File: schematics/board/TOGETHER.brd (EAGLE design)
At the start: 22 x 22 mm, 12 parts

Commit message: Добавлена плата TOGETHER
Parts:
- added U$1, U$18, U$19, U$2, U$20, U$21, U$3, U$4: KCONNECT-, CanCubeSat:KCONNECT-
- moved 3V3 42.4 mm to (39.5, 32.5)
- moved C1 42.4 mm to (32.5, 38.5)
- moved C10 42.4 mm to (35.0, 38.5)
- moved LIS3MDL 42.4 mm to (33.0, 43.0)
- moved LSM6DS3 42.4 mm to (49.0, 43.0)
- moved PWR 42.4 mm to (41.0, 49.0)
- moved R1 42.4 mm to (41.0, 47.0)
- moved R101 42.4 mm to (47.0, 38.5)
- moved R102 42.4 mm to (49.5, 38.5)
- moved SCL 42.4 mm to (42.5, 32.5)
- moved GND 42.4 mm to (36.5, 33.8)
- moved SDA 42.4 mm to (45.5, 33.8)
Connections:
- net GND renamed GND1
- new net BUS+: U$1.1, U$1.2, U$1.3, U$1.4, U$18.1, U$18.2, U$18.3, U$18.4, U$20.1, U$20.2, U$20.3, U$20.4, U$3.1, U$3.2, U$3.3, U$3.4
- new net BUS-: U$19.1, U$19.2, U$19.3, U$19.4, U$2.1, U$2.2, U$2.3, U$2.4, U$21.1, U$21.2, U$21.3, U$21.4, U$4.1, U$4.2, U$4.3, U$4.4
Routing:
- net GND1: track 51.8 -> 22.0 mm
- net VDD: track 59.9 -> 56.7 mm
- added copper zone on layer 16, net BUS+
- added copper zone on layer 1, net BUS-
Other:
- board size 22 x 22 mm -> 82 x 82 mm

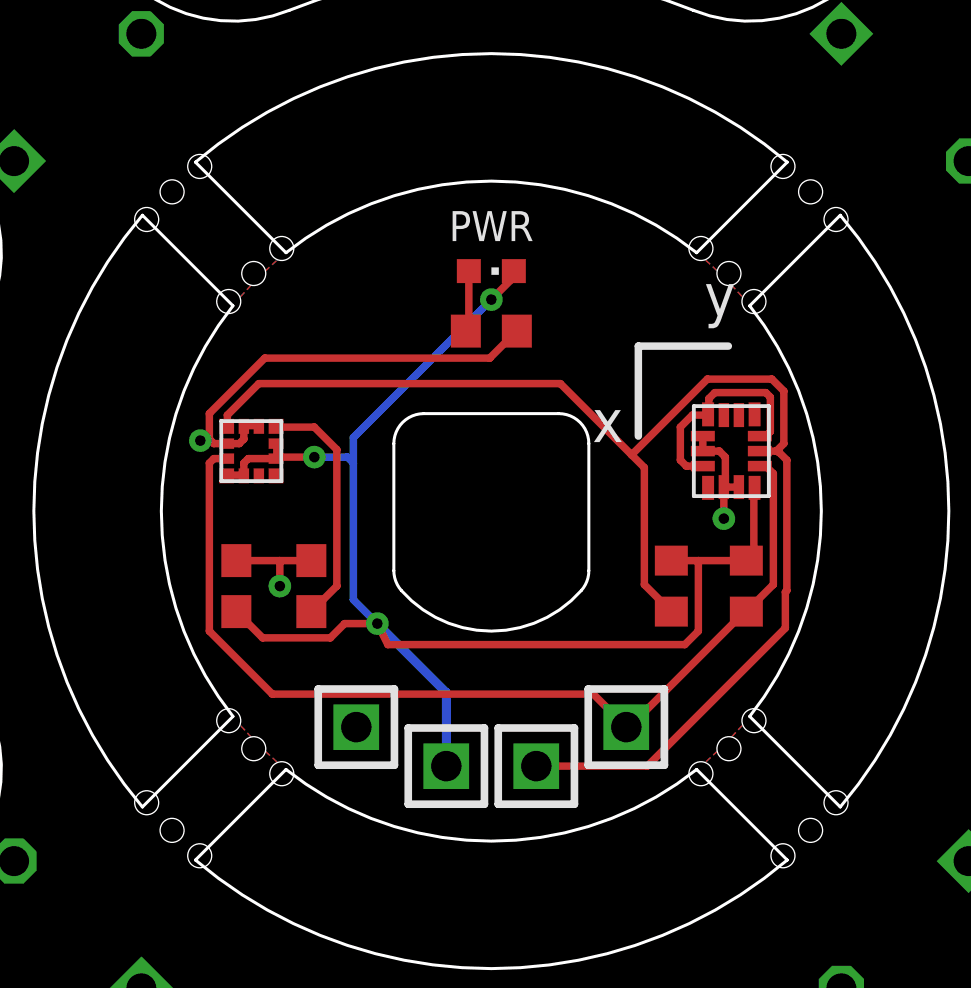
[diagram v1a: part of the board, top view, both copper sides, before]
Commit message: Исправлены MAG и BSK1
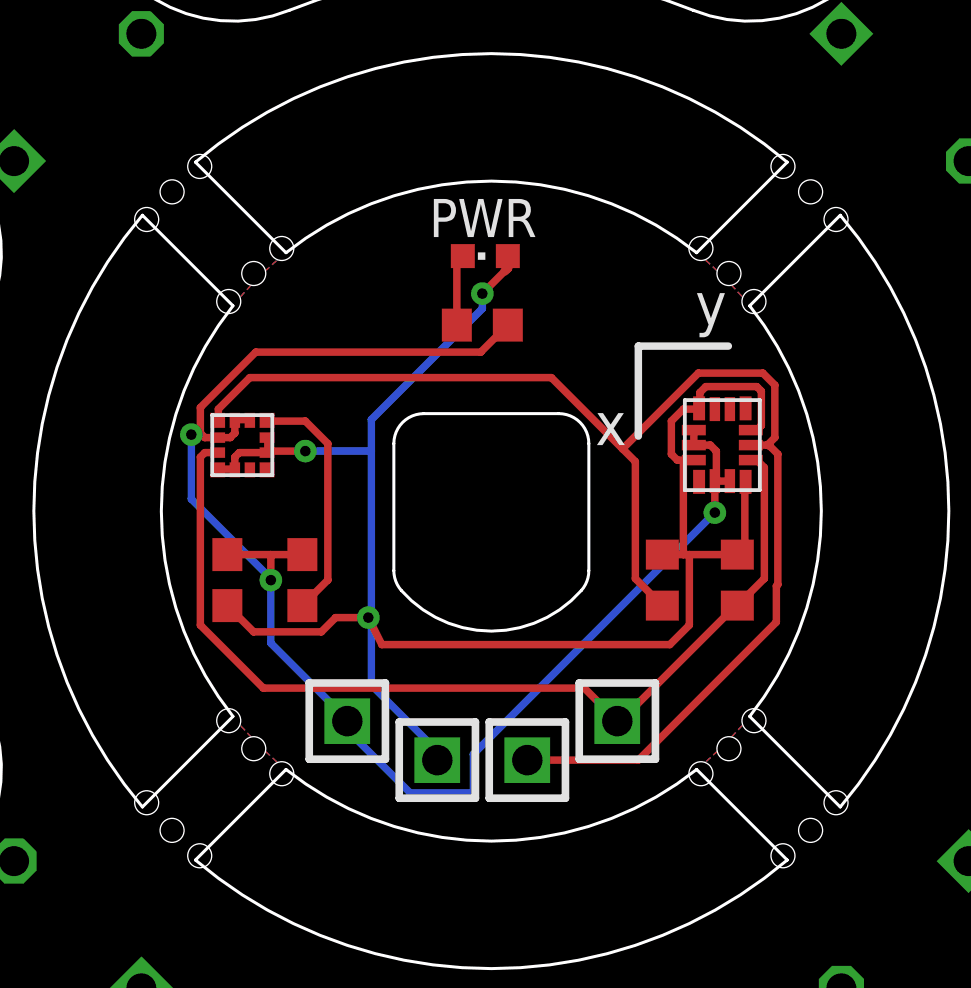
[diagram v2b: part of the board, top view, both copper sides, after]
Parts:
- moved PWR 0.54 mm to (40.8, 49.5), turned to 90 degrees
- moved 3V3 0.36 mm to (39.2, 32.7)
- moved C1 0.36 mm to (32.2, 38.7)
- moved C10 0.36 mm to (34.7, 38.7)
- moved GND 0.36 mm to (36.2, 34.0)
- moved LIS3MDL 0.36 mm to (32.7, 43.2)
- moved LSM6DS3 0.36 mm to (48.7, 43.2)
- moved R1 0.36 mm to (40.7, 47.2)
- moved R101 0.36 mm to (46.7, 38.7)
- moved R102 0.36 mm to (49.2, 38.7)
- moved SCL 0.36 mm to (42.2, 32.7)
- moved SDA 0.36 mm to (45.2, 34.0)
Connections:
- net GND1 renamed GND
- removed net N$37: PWR.A, R1.2
- removed net VDD: 3V3.1, C1.1, LIS3MDL.P$1, LIS3MDL.P$2, LIS3MDL.P$5, LIS3MDL.P$6, LSM6DS3.P$11, LSM6DS3.P$14, LSM6DS3.P$4, LSM6DS3.P$7, PWR.C, R101.1, R102.1
- new net N$1: PWR.C, R1.2
- new net VDD1: 3V3.1, C1.1, LIS3MDL.P$1, LIS3MDL.P$2, LIS3MDL.P$5, LIS3MDL.P$6, LSM6DS3.P$11, LSM6DS3.P$14, LSM6DS3.P$4, LSM6DS3.P$7, PWR.A, R101.1, R102.1
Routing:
- net VDD1: track 0.00 -> 60.4 mm, vias 0 -> 3
- net VDD: track 56.7 -> 0.00 mm, vias 3 -> 0
- net GND: track 22.0 -> 51.9 mm
- net N$1: track 0.00 -> 2.38 mm
- net N$37: track 2.04 -> 0.00 mm
- added copper zone on layer 1, net VDD1
- removed copper zone on layer 1, net VDD
